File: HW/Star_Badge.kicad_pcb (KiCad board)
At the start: 2 copper layers, 180 x 171.6 mm, 55 parts, among them J1 AVR-ISP-6, J2 10118194-0001LF, Q1 Q_NMOS_DGS, Q2 Q_PMOS_DGS, U1 ATTINY861-15XD, U2 TPS613221ADBVT, U3 AP7363-33D-13, X1 Badgelife_sao_connector_v169b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, X2 Badgelife_sao_connector_v169b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, X3 Badgelife_sao_connector_v169b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

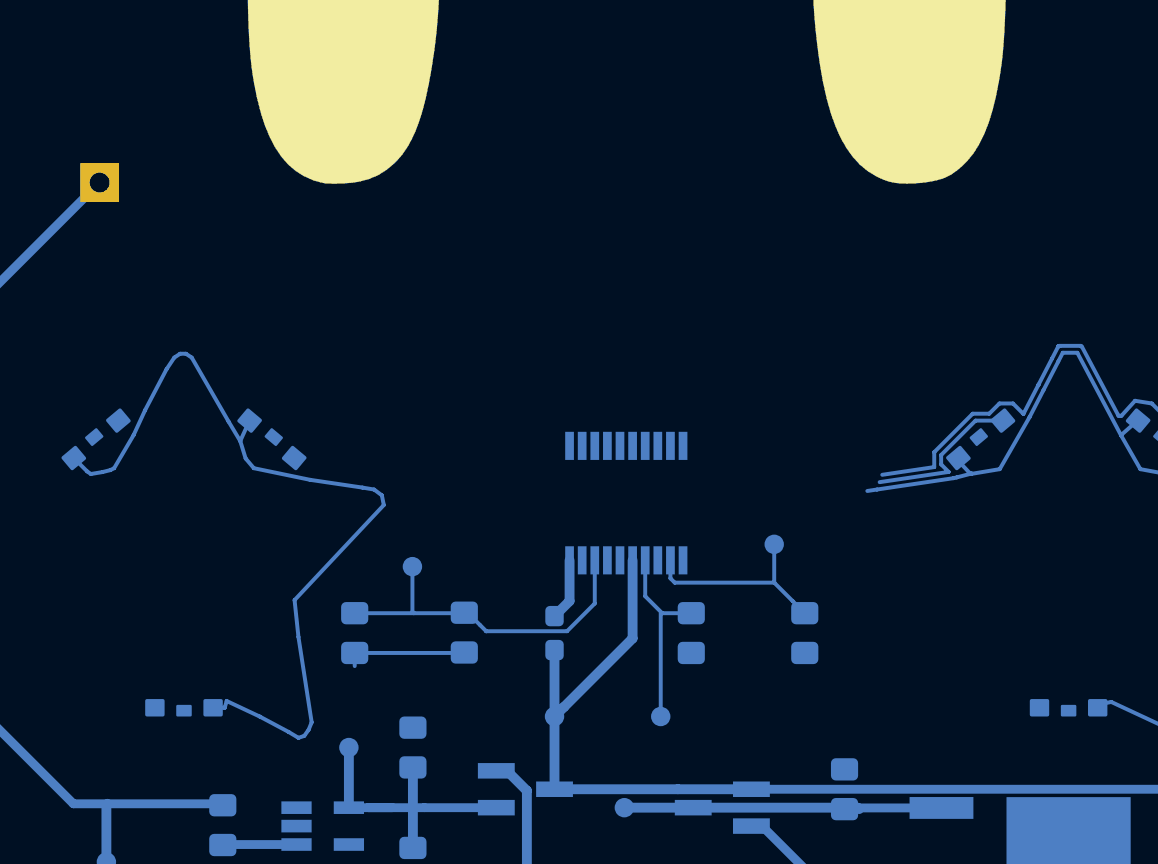
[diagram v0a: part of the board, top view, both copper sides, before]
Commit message: Star 4 routing
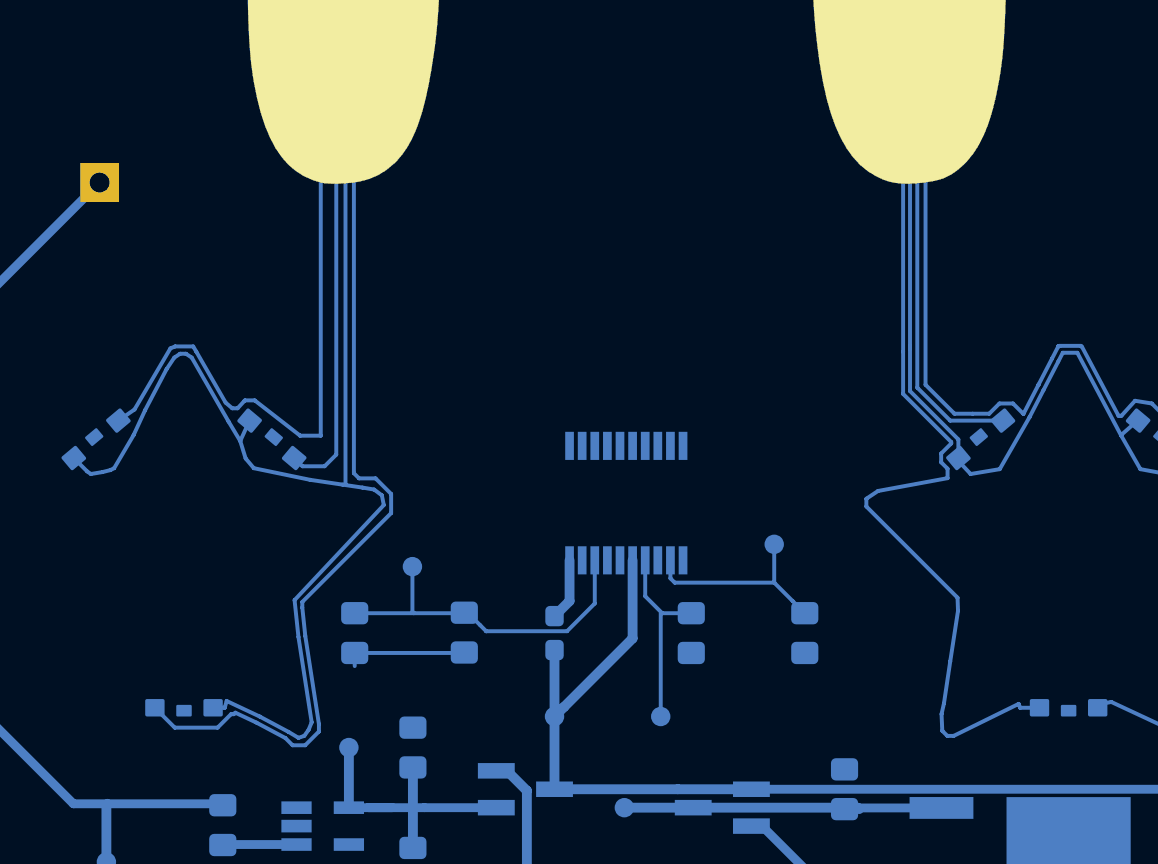
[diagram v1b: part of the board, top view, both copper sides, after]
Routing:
- net /B_LED_BUS: track 55.5 -> 141.6 mm
- net /G_LED_BUS: track 162.2 -> 200.5 mm
- net /R_LED_BUS: track 156.3 -> 184.0 mm
- net /EN_RGB2: track 44.4 -> 62.6 mm
- net /EN_RGB3: track 49.8 -> 60.7 mm

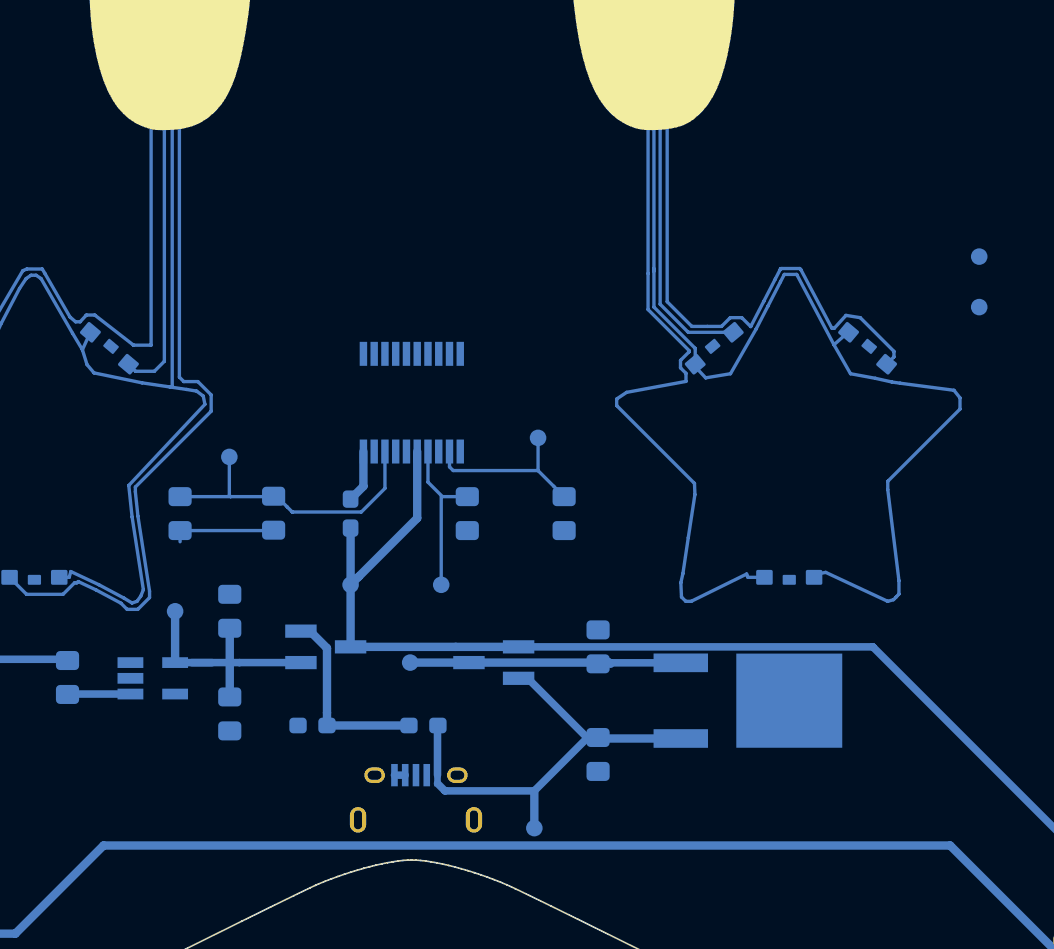
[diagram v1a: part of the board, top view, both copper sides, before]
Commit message: deleted power routign to get ground pour.
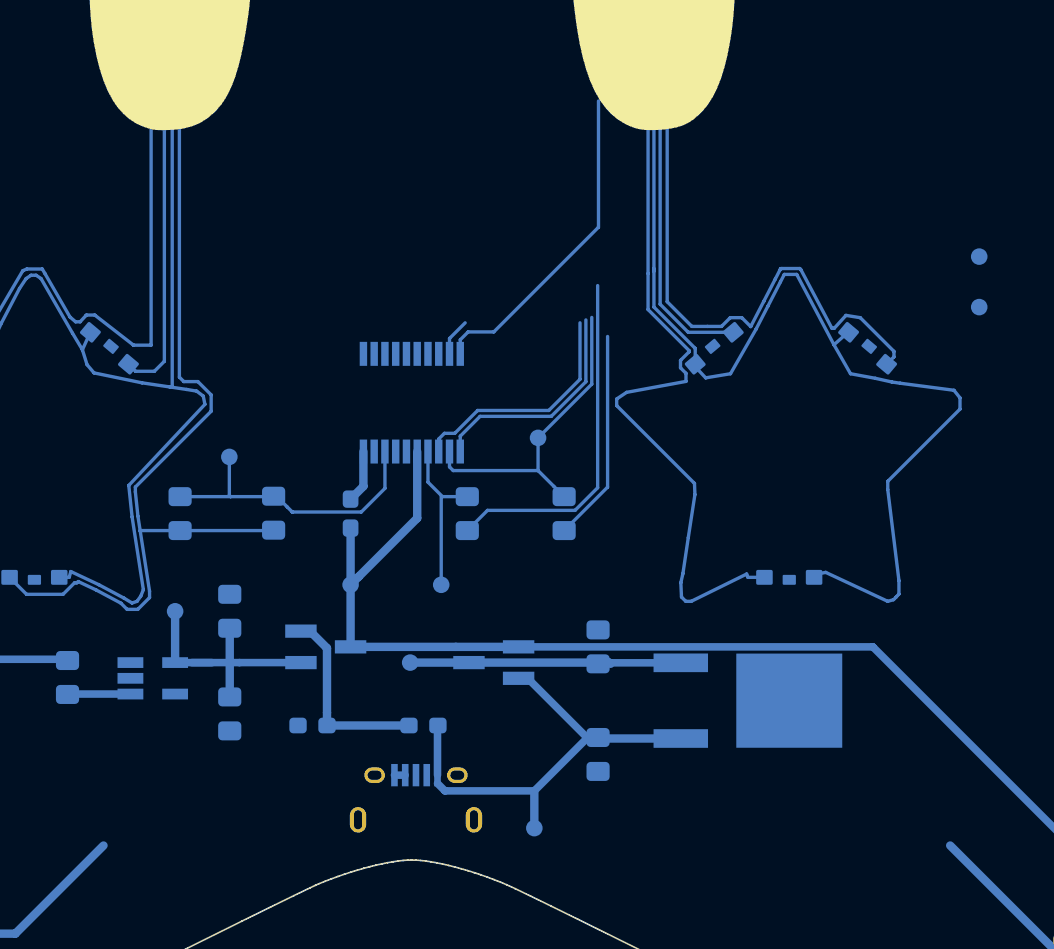
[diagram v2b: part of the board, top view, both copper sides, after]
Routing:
- net /VBUS: track 335.1 -> 284.0 mm
- net /G_LED_BUS: track 200.5 -> 221.7 mm
- net /GPIO_1_1: track 0.00 -> 19.6 mm
- net /SCL_SCK: track 0.00 -> 14.2 mm
- net /SDA_MOSI: track 0.00 -> 13.6 mm
- net /R_LED_BUS: track 184.0 -> 196.8 mm
- net /R_PWM__MISO: track 10.6 -> 19.2 mm
- net /GPIO_1_2: track 0.00 -> 2.27 mm
- net /B_LED_BUS: track 141.6 -> 143.3 mm
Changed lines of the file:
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@@
     (thickness 1.6)
     (drawings 611)
-    (tracks 596)
+    (tracks 624)
     (zones 0)
     (modules 55)
@@
   (segment (start 84.448507 131.101493) (end 85.05 130.5) (width 0.2032) (layer B.Cu) (net 6))
   (segment (start 85.05 130.5) (end 85.05 113.625) (width 0.2032) (layer B.Cu) (net 6))
+  (segment (start 109.2 140.725) (end 111.825 138.1) (width 0.2032) (layer B.Cu) (net 6))
+  (segment (start 111.825 138.1) (end 111.825 129) (width 0.2032) (layer B.Cu) (net 6))
   (segment (start 98.9 56.425887) (end 99.6 55.1) (width 0.2032) (layer B.Cu) (net 7))
   (segment (start 97.4 59.3) (end 98.9 56.425887) (width 0.2032) (layer B.Cu) (net 7))
@@
   (segment (start 84.25 114.625) (end 84.25 129.525) (width 0.2032) (layer B.Cu) (net 8))
   (segment (start 83.180798 129.519202) (end 80.845438 127.704562) (width 0.2032) (layer B.Cu) (net 8))
+  (segment (start 109.85877 139.50401) (end 111.225 138.13778) (width 0.2032) (layer B.Cu) (net 8))
+  (segment (start 103.35 140.725) (end 104.57099 139.50401) (width 0.2032) (layer B.Cu) (net 8))
+  (segment (start 104.57099 139.50401) (end 109.85877 139.50401) (width 0.2032) (layer B.Cu) (net 8))
+  (segment (start 111.225 138.13778) (end 111.225 125.925) (width 0.2032) (layer B.Cu) (net 8))
   (segment (start 91.85 140.725) (end 86 140.725) (width 0.2032) (layer B.Cu) (net 9))
-  (segment (start 86 141.4) (end 86 140.725) (width 0.2032) (layer B.Cu) (net 9))
   (segment (start 98.5 73.3) (end 98.5 80.425) (width 0.2032) (layer B.Cu) (net 9))
   (segment (start 61.6 100.15) (end 61.6 100.7) (width 0.2032) (layer B.Cu) (net 9))
@@
   (segment (start 87.877591 133.515987) (end 87.877591 132.527591) (width 0.2032) (layer B.Cu) (net 9))
   (segment (start 83.452745 139.85412) (end 83.29845 138.388321) (width 0.2032) (layer B.Cu) (net 9))
-  (segment (start 84.155526 144.391128) (end 83.452745 139.85412) (width 0.2032) (layer B.Cu) (net 9))
   (segment (start 79.768494 143.881506) (end 79.846749 143.803252) (width 0.2032) (layer B.Cu) (net 9))
   (segment (start 86.225 131.725) (end 85.957812 131.457812) (width 0.2032) (layer B.Cu) (net 9))
@@
   (segment (start 82.424731 145.109547) (end 82.799124 145.48394) (width 0.2032) (layer B.Cu) (net 9))
   (segment (start 84.155526 144.774971) (end 84.155526 144.391128) (width 0.2032) (layer B.Cu) (net 9))
+  (segment (start 84.155526 144.391128) (end 83.589302 140.735698) (width 0.2032) (layer B.Cu) (net 9))
+  (segment (start 83.589302 140.735698) (end 83.452745 139.85412) (width 0.2032) (layer B.Cu) (net 9))
+  (segment (start 83.6 140.725) (end 83.589302 140.735698) (width 0.2032) (layer B.Cu) (net 9))
+  (segment (start 86 140.725) (end 83.6 140.725) (width 0.2032) (layer B.Cu) (net 9))
   (segment (start 69.7 101.2) (end 69.7 100.9) (width 0.2032) (layer B.Cu) (net 10))
   (segment (start 69.4 101.6) (end 69.7 101.2) (width 0.2032) (layer B.Cu) (net 10))
@@
   (segment (start 102.275 136.8782) (end 102.4968 137.1) (width 0.2032) (layer B.Cu) (net 14))
   (segment (start 107.625 137.1) (end 107.625 135.125) (width 0.2032) (layer B.Cu) (net 14))
+  (segment (start 107.625 135.125) (end 110.86939 131.88061) (width 0.2032) (layer B.Cu) (net 14))
+  (segment (start 110.86939 131.88061) (end 110.86939 127.85) (width 0.2032) (layer B.Cu) (net 14))
   (segment (start 102.6572 147.75) (end 106.45 147.75) (width 0.508) (layer B.Cu) (net 15))
   (segment (start 102.6572 147.75) (end 96.3 147.75) (width 0.508) (layer B.Cu) (net 15))
@@
   (segment (start 26.383599 79.691401) (end 30.625 75.45) (width 0.508) (layer B.Cu) (net 15))
   (segment (start 30.625 75.45) (end 63.225 75.45) (width 0.508) (layer B.Cu) (net 15))
-  (segment (start 132.52 159.75) (end 81.375 159.75) (width 0.508) (layer B.Cu) (net 15))
   (segment (start 81.375 159.75) (end 76.05 165.075) (width 0.508) (layer B.Cu) (net 15))
   (segment (start 76.05 165.075) (end 57.195 165.075) (width 0.508) (layer B.Cu) (net 15))
@@
   (segment (start 57.195 124.57) (end 57.195 165.075) (width 0.508) (layer B.Cu) (net 15))
   (segment (start 24.249999 91.624999) (end 57.195 124.57) (width 0.508) (layer B.Cu) (net 15))
+  (segment (start 101.967798 134.85) (end 102.593892 134.85) (width 0.2032) (layer B.Cu) (net 16))
+  (segment (start 101.625 135.95) (end 101.625 135.192798) (width 0.2032) (layer B.Cu) (net 16))
+  (segment (start 101.625 135.192798) (end 101.967798 134.85) (width 0.2032) (layer B.Cu) (net 16))
+  (segment (start 102.593892 134.85) (end 103.974502 133.46939) (width 0.2032) (layer B.Cu) (net 16))
+  (segment (start 103.974502 133.46939) (end 108.274794 133.46939) (width 0.2032) (layer B.Cu) (net 16))
+  (segment (start 108.274794 133.46939) (end 110.15817 131.586014) (width 0.2032) (layer B.Cu) (net 16))
+  (segment (start 110.15817 131.586014) (end 110.15817 128.175) (width 0.2032) (layer B.Cu) (net 16))
+  (segment (start 102.925 135.0218) (end 104.1218 133.825) (width 0.2032) (layer B.Cu) (net 17))
+  (segment (start 102.925 135.95) (end 102.925 135.0218) (width 0.2032) (layer B.Cu) (net 17))
+  (segment (start 104.1218 133.825) (end 108.422092 133.825) (width 0.2032) (layer B.Cu) (net 17))
+  (segment (start 108.422092 133.825) (end 110.51378 131.733312) (width 0.2032) (layer B.Cu) (net 17))
+  (segment (start 110.51378 131.733312) (end 110.51378 128) (width 0.2032) (layer B.Cu) (net 17))
   (segment (start 97.075 138.05) (end 96.3 138.825) (width 0.508) (layer B.Cu) (net 18))
   (segment (start 97.075 135.95) (end 97.075 138.05) (width 0.508) (layer B.Cu) (net 18))
@@
   (segment (start 91.85 138.675) (end 89.05 138.675) (width 0.2032) (layer B.Cu) (net 22))
   (segment (start 58.725 111.75) (end 54.475 111.75) (width 0.508) (layer B.Cu) (net 23))
+  (segment (start 102.925 129.2) (end 103.4 128.725) (width 0.2032) (layer B.Cu) (net 24))
+  (segment (start 102.925 130.05) (end 102.925 129.2) (width 0.2032) (layer B.Cu) (net 24))
+  (segment (start 103.4 128.725) (end 104.95 128.725) (width 0.2032) (layer B.Cu) (net 24))
+  (segment (start 104.95 128.725) (end 111.275 122.4) (width 0.2032) (layer B.Cu) (net 24))
+  (segment (start 111.275 122.4) (end 111.275 114.775) (width 0.2032) (layer B.Cu) (net 24))
+  (segment (start 102.275 129.1218) (end 103.2218 128.175) (width 0.2032) (layer B.Cu) (net 25))
+  (segment (start 102.275 130.05) (end 102.275 129.1218) (width 0.2032) (layer B.Cu) (net 25))
   (zone (net 0) (net_name "") (layers F&B.Cu) (hatch full 0.508)
     (connect_pads (clearance 0.508))

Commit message: moved button, Previous commit had i2c routign
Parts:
- moved S1 0.60 mm to (56.0, 110.0), turned to 90 degrees
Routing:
- net /VBUS: track 284.0 -> 237.4 mm
- net /Button: track 4.25 -> 29.6 mm
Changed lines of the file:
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@@
     (thickness 1.6)
     (drawings 611)
-    (tracks 624)
+    (tracks 625)
     (zones 0)
     (modules 55)
@@
       (net 1 GND))
   )
-  (module digikey-footprints:Switch_Tactile_SMD_4.5x4.5mm_TL3315NF160Q (layer B.Cu)
-    (at 56.6 110)
+  (module digikey-footprints:Switch_Tactile_SMD_4.5x4.5mm_TL3315NF160Q locked (layer B.Cu)
+    (at 56 110 90)
     (descr http://spec_sheets.e-switch.com/specs/P010337.pdf)
     (attr smd)
-    (fp_text reference S1 (at 0 3.31) (layer B.SilkS)
+    (fp_text reference S1 (at 0 3.31 90) (layer B.SilkS)
       (effects (font (size 1 1) (thickness 0.15)) (justify mirror))
     )
-    (fp_text value TL3315NF160Q (at 0 -3.58) (layer B.Fab)
+    (fp_text value TL3315NF160Q (at 0 -3.58 90) (layer B.Fab)
       (effects (font (size 1 1) (thickness 0.15)) (justify mirror))
     )
@@
     (fp_line (start 2.25 2.25) (end -2.25 2.25) (layer B.Fab) (width 0.1))
     (fp_line (start -2.25 -2.25) (end 2.25 -2.25) (layer B.Fab) (width 0.1))
-    (fp_text user %R (at 0 0) (layer B.Fab)
+    (fp_text user %R (at 0 0 90) (layer B.Fab)
       (effects (font (size 1 1) (thickness 0.15)) (justify mirror))
     )
@@
     (fp_line (start -2.83 2.5) (end 2.83 2.5) (layer B.CrtYd) (width 0.05))
     (fp_line (start -2.83 -2.5) (end 2.83 -2.5) (layer B.CrtYd) (width 0.05))
-    (pad 4 smd rect (at 2.125 -1.75) (size 0.5 0.7) (layers B.Cu B.Paste B.Mask)
+    (pad 4 smd rect (at 2.125 -1.75 90) (size 0.5 0.7) (layers B.Cu B.Paste B.Mask)
       (net 1 GND))
-    (pad 3 smd rect (at -2.125 -1.75) (size 0.5 0.7) (layers B.Cu B.Paste B.Mask)
+    (pad 3 smd rect (at -2.125 -1.75 90) (size 0.5 0.7) (layers B.Cu B.Paste B.Mask)
       (net 1 GND))
-    (pad 2 smd rect (at 2.125 1.75) (size 0.5 0.7) (layers B.Cu B.Paste B.Mask)
+    (pad 2 smd rect (at 2.125 1.75 90) (size 0.5 0.7) (layers B.Cu B.Paste B.Mask)
       (net 23 /Button))
-    (pad 1 smd rect (at -2.125 1.75) (size 0.5 0.7) (layers B.Cu B.Paste B.Mask)
+    (pad 1 smd rect (at -2.125 1.75 90) (size 0.5 0.7) (layers B.Cu B.Paste B.Mask)
       (net 23 /Button))
-    (pad 2 smd rect (at 2.475 1.75) (size 0.2 1.1) (layers B.Cu B.Paste B.Mask)
+    (pad 2 smd rect (at 2.475 1.75 90) (size 0.2 1.1) (layers B.Cu B.Paste B.Mask)
       (net 23 /Button))
-    (pad 3 smd rect (at -2.475 -1.75) (size 0.2 1.1) (layers B.Cu B.Paste B.Mask)
+    (pad 3 smd rect (at -2.475 -1.75 90) (size 0.2 1.1) (layers B.Cu B.Paste B.Mask)
       (net 1 GND))
-    (pad 4 smd rect (at 2.475 -1.75) (size 0.2 1.1) (layers B.Cu B.Paste B.Mask)
+    (pad 4 smd rect (at 2.475 -1.75 90) (size 0.2 1.1) (layers B.Cu B.Paste B.Mask)
       (net 1 GND))
-    (pad 1 smd rect (at -2.475 1.75) (size 0.2 1.1) (layers B.Cu B.Paste B.Mask)
+    (pad 1 smd rect (at -2.475 1.75 90) (size 0.2 1.1) (layers B.Cu B.Paste B.Mask)
       (net 23 /Button))
     (model ${KIPRJMOD}/Star_Badge.pretty/TL3315NFxxxQ.stp
@@
   (segment (start 25.52 84.75) (end 24.249999 86.020001) (width 0.508) (layer B.Cu) (net 15))
   (segment (start 57.195 124.57) (end 57.195 165.075) (width 0.508) (layer B.Cu) (net 15))
-  (segment (start 24.249999 91.624999) (end 57.195 124.57) (width 0.508) (layer B.Cu) (net 15))
   (segment (start 101.967798 134.85) (end 102.593892 134.85) (width 0.2032) (layer B.Cu) (net 16))
   (segment (start 101.625 135.95) (end 101.625 135.192798) (width 0.2032) (layer B.Cu) (net 16))
@@
   (segment (start 89.05 138.675) (end 86 138.675) (width 0.2032) (layer B.Cu) (net 22))
   (segment (start 91.85 138.675) (end 89.05 138.675) (width 0.2032) (layer B.Cu) (net 22))
-  (segment (start 58.725 111.75) (end 54.475 111.75) (width 0.508) (layer B.Cu) (net 23))
+  (segment (start 57.725 110.3) (end 83.1 110.3) (width 0.2032) (layer B.Cu) (net 23))
+  (segment (start 57.725 110.3) (end 57.725 112.15) (width 0.508) (layer B.Cu) (net 23))
+  (segment (start 57.725 107.9) (end 57.725 110.3) (width 0.508) (layer B.Cu) (net 23))
   (segment (start 102.925 129.2) (end 103.4 128.725) (width 0.2032) (layer B.Cu) (net 24))
   (segment (start 102.925 130.05) (end 102.925 129.2) (width 0.2032) (layer B.Cu) (net 24))
